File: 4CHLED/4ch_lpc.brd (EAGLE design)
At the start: 37.7 x 53.9 mm, 52 parts, among them IC1 LT1761, IC2 MAX487CSA, IC3 LT3972, IC4 78L05SMD, Q1 MT-OSCILLATOR, T1 IRF7103, T2 IRF7103, X1 RJ45-8L-B, X2 RJ45-8L-B, X4 87758-0616

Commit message: final touches for production
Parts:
- added R17: 68k, SparkFun:0402-RES
- renumbered U1 to IC5
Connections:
- net !RE: now also R17.2
- net +3V3: now also IC5.P$9
- net GND: now also R17.1
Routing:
- net !RE: track 26.5 -> 30.8 mm
- net +3V3: track 40.2 -> 42.7 mm
- net GND: vias 49 -> 57

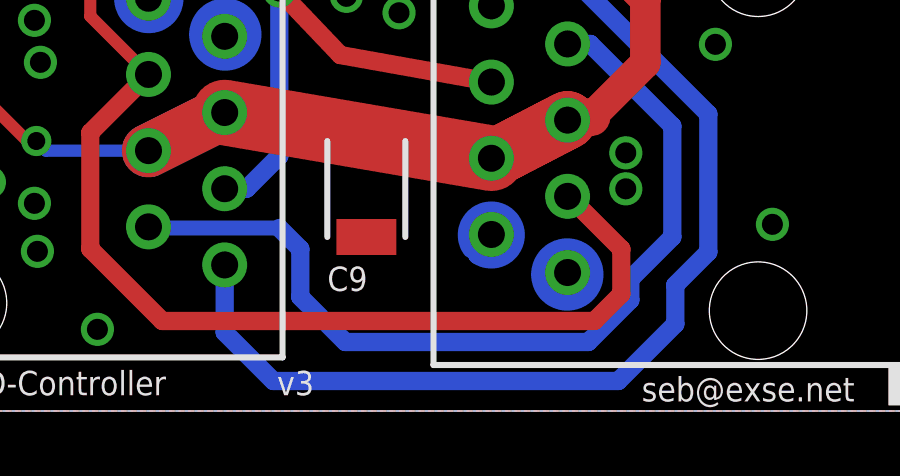
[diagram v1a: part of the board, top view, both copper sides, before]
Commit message: rs485 shielding
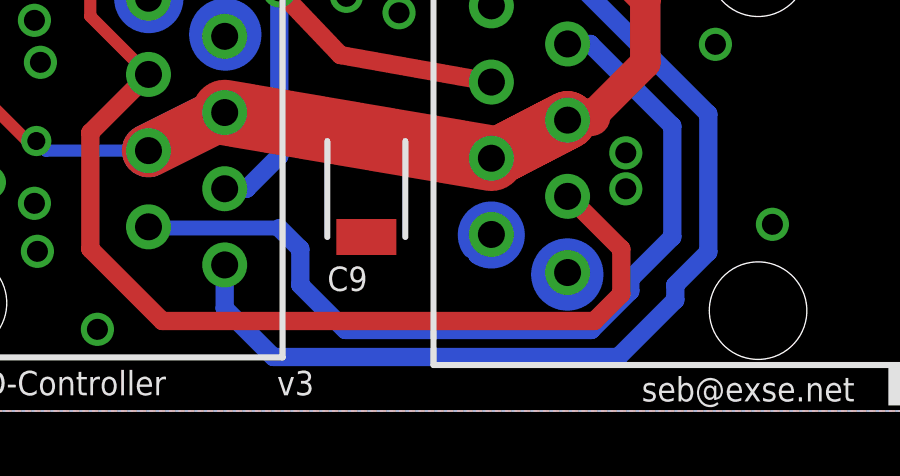
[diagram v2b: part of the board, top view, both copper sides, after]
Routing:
- net N$19: track 35.4 -> 33.8 mm
- net N$18: track 30.2 -> 29.4 mm
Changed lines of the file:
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@@
 <grid distance="0.1" unitdist="mm" unit="mm" style="dots" multiple="1" display="yes" altdistance="0.025" altunitdist="inch" altunit="inch"/>
 <layers>
-<layer number="1" name="Top" color="4" fill="1" visible="yes" active="yes"/>
+<layer number="1" name="Top" color="4" fill="1" visible="no" active="yes"/>
 <layer number="2" name="Route2" color="1" fill="3" visible="no" active="no"/>
 <layer number="3" name="Route3" color="4" fill="3" visible="no" active="no"/>
@@
 <layer number="14" name="Route14" color="1" fill="6" visible="no" active="no"/>
 <layer number="15" name="Route15" color="4" fill="6" visible="no" active="no"/>
-<layer number="16" name="Bottom" color="1" fill="1" visible="no" active="yes"/>
+<layer number="16" name="Bottom" color="1" fill="1" visible="yes" active="yes"/>
 <layer number="17" name="Pads" color="2" fill="1" visible="yes" active="yes"/>
 <layer number="18" name="Vias" color="2" fill="1" visible="yes" active="yes"/>
@@
 <wire x1="37.4" y1="-12.5" x2="37.4" y2="-8.8" width="0.6096" layer="16"/>
 <wire x1="36" y1="-13.9" x2="37.4" y2="-12.5" width="0.6096" layer="16"/>
-<wire x1="36" y1="-14.6" x2="36" y2="-13.9" width="0.6096" layer="16"/>
-<wire x1="34.6" y1="-16" x2="36" y2="-14.6" width="0.6096" layer="16"/>
+<wire x1="36" y1="-14.3" x2="36" y2="-13.9" width="0.6096" layer="16"/>
+<wire x1="34.7" y1="-15.6" x2="36" y2="-14.3" width="0.6096" layer="16"/>
 <wire x1="19.939" y1="-12.161" x2="19.978" y2="-12.2" width="0.6096" layer="16"/>
 <wire x1="19.978" y1="-12.2" x2="24.3" y2="-12.2" width="0.5" layer="16"/>
 <wire x1="24.3" y1="-12.2" x2="25" y2="-12.9" width="0.6096" layer="16"/>
-<wire x1="25" y1="-12.9" x2="25" y2="-14.5" width="0.6096" layer="16"/>
-<wire x1="25" y1="-14.5" x2="26.5" y2="-16" width="0.6096" layer="16"/>
-<wire x1="26.5" y1="-16" x2="34.6" y2="-16" width="0.6096" layer="16"/>
+<wire x1="25" y1="-12.9" x2="25" y2="-14.1" width="0.6096" layer="16"/>
+<wire x1="25" y1="-14.1" x2="26.5" y2="-15.6" width="0.6096" layer="16"/>
+<wire x1="26.5" y1="-15.6" x2="34.7" y2="-15.6" width="0.6096" layer="16"/>
 </signal>
 <signal name="N$19">
@@
 <wire x1="38.6" y1="-8.4" x2="34.4" y2="-4.2" width="0.6096" layer="16"/>
 <wire x1="38.6" y1="-13" x2="38.6" y2="-8.4" width="0.6096" layer="16"/>
-<wire x1="22.479" y1="-15.679" x2="24.1" y2="-17.3" width="0.6096" layer="16"/>
-<wire x1="22.479" y1="-15.679" x2="22.479" y2="-13.431" width="0.6096" layer="16"/>
+<wire x1="22.479" y1="-14.879" x2="24.1" y2="-16.5" width="0.6096" layer="16"/>
+<wire x1="22.479" y1="-14.879" x2="22.479" y2="-13.431" width="0.6096" layer="16"/>
 <wire x1="37.5" y1="-14.1" x2="38.6" y2="-13" width="0.6096" layer="16"/>
-<wire x1="37.5" y1="-15.4" x2="37.5" y2="-14.1" width="0.6096" layer="16"/>
-<wire x1="35.6" y1="-17.3" x2="37.5" y2="-15.4" width="0.6096" layer="16"/>
-<wire x1="24.1" y1="-17.3" x2="35.6" y2="-17.3" width="0.6096" layer="16"/>
+<wire x1="37.5" y1="-14.6" x2="37.5" y2="-14.1" width="0.6096" layer="16"/>
+<wire x1="35.6" y1="-16.5" x2="37.5" y2="-14.6" width="0.6096" layer="16"/>
+<wire x1="24.1" y1="-16.5" x2="35.6" y2="-16.5" width="0.6096" layer="16"/>
 </signal>
 <signal name="TXD">
